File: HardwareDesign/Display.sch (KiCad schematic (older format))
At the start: 1 part, among them U601 Upduino_3.0

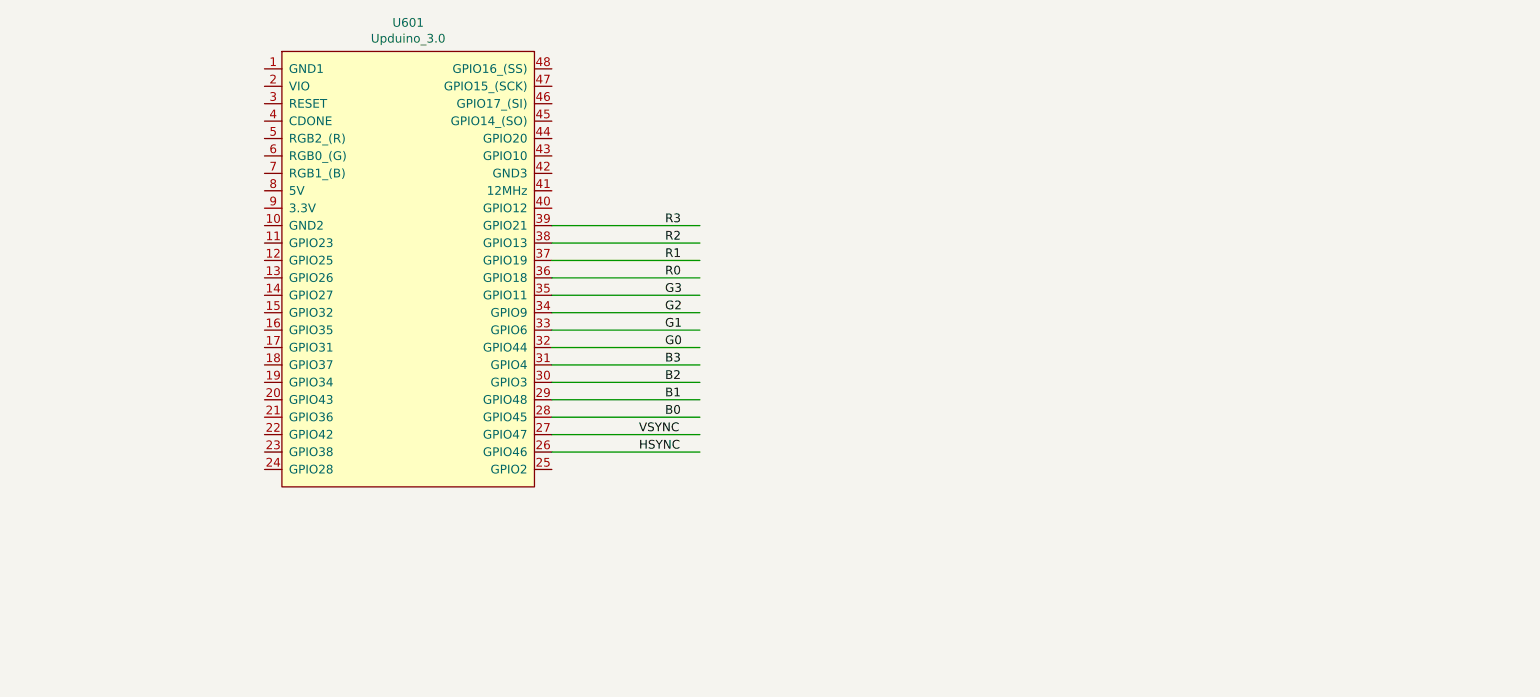
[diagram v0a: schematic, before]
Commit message: initial display circuit
The display isn't interfaced with the system yet.
Initial goal is to generate a valid 800x600 SVGA signal.

Added a footprint for the Upduino 3.0, which is DIP-48,
but 0.7" wide rather than the standard 0.6".
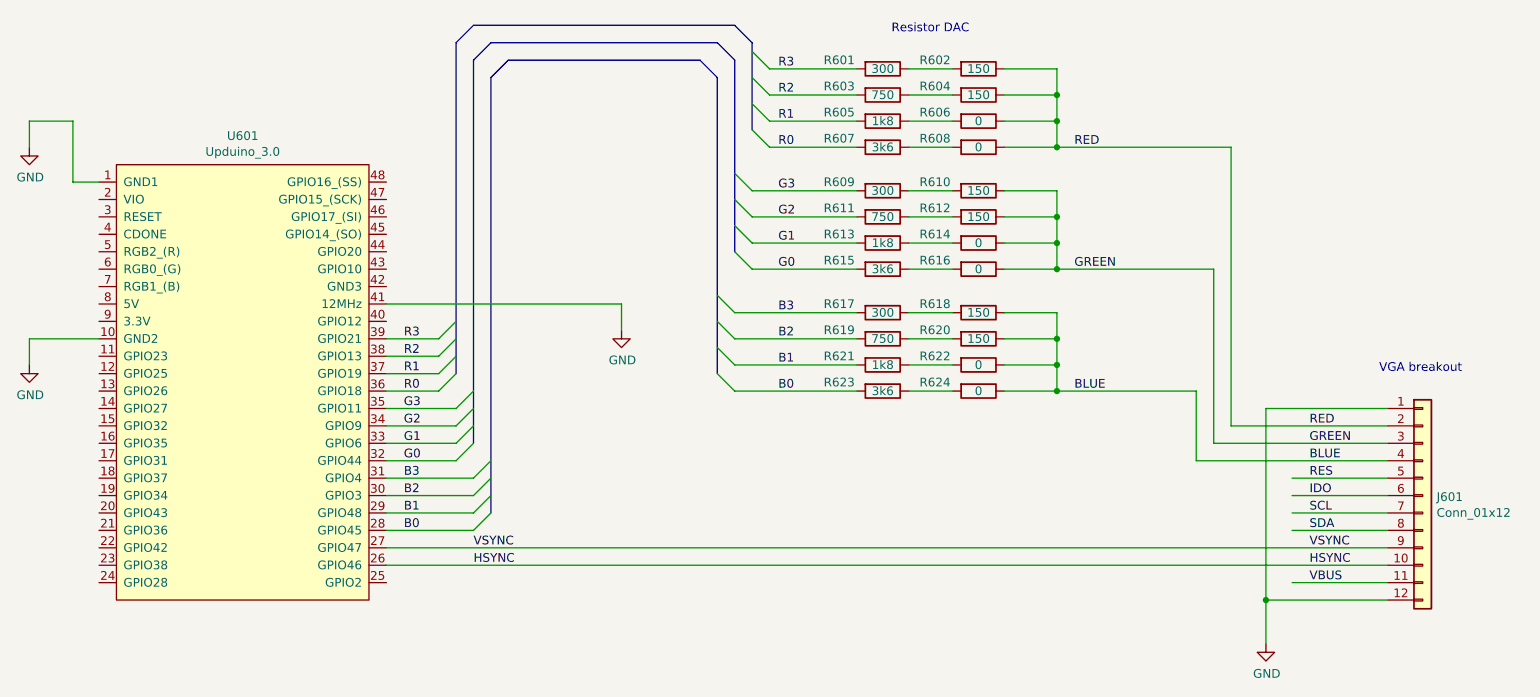
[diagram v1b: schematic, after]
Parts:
- added J601: Conn_01x12, symbol Connector_Generic:Conn_01x12
- added R601, R609, R617: 300, symbol device:R
- added R602, R604, R610, R612, R618, R620: 150, symbol device:R
- added R603, R611, R619: 750, symbol device:R
- added R605, R613, R621: 1k8, symbol device:R
- added R606, R608, R614, R616, R622, R624: 0, symbol device:R
- added R607, R615, R623: 3k6, symbol device:R
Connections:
- net labels added: BLUE, GND, GREEN, IDO, RED, RES, SCL, SDA, VBUS
- wire segments 14 -> 85
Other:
- note added: "Resistor DAC"
- note added: "VGA breakout"
- moved on the sheet: U601

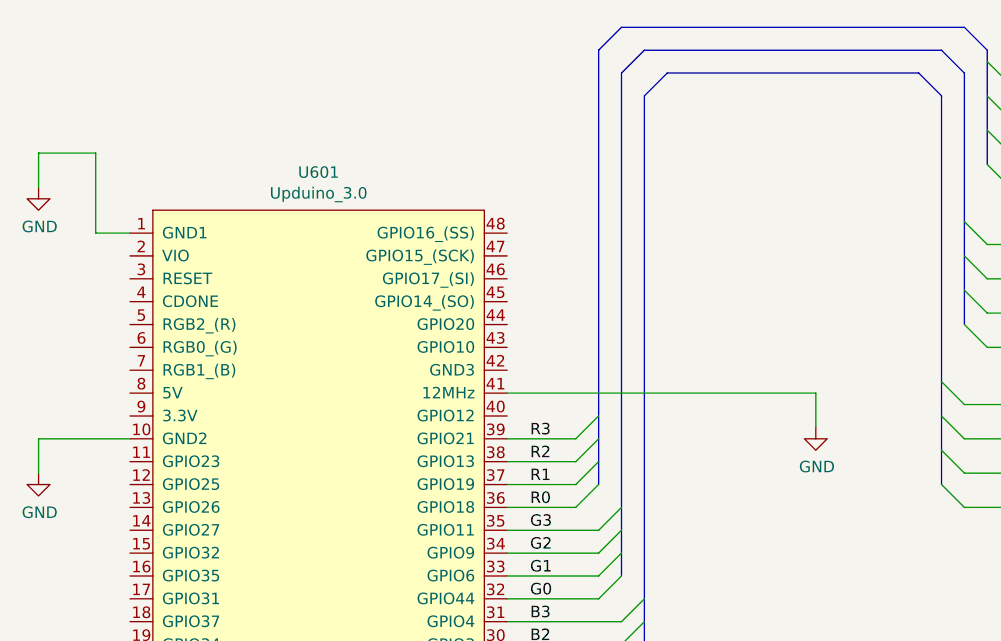
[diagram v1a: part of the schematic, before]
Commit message: corrected Upduino 3.0 pin assignments
The 12MHz and GND3 pins were accidentally reversed
on the silkscreen.
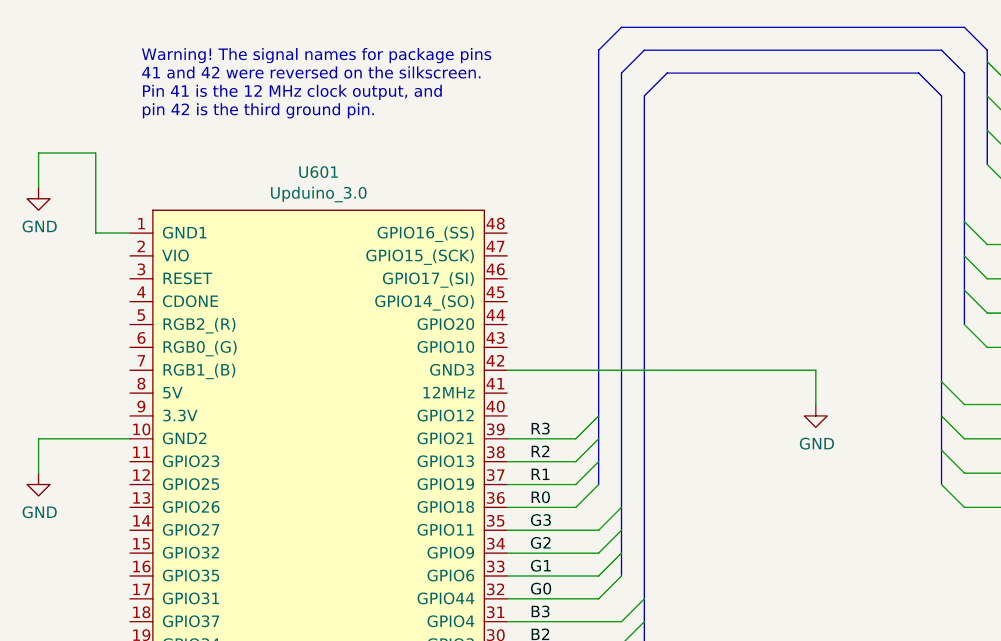
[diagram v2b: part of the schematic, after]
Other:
- note added: "Warning! The signal names for package pins\n41 and 42 were reversed on the silkscreen.\nPin 41 is the 12 MHz clock output, and\npin 42 is the third ground pin."
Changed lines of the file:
@@
 Comment4 ""
 $EndDescr
-$Comp
-L Upduino_3.0:Upduino_3.0 U601
-U 1 1 60B8636D
-P 2400 2400
-F 0 "U601" H 2375 2465 50  0000 C CNN
-F 1 "Upduino_3.0" H 2375 2374 50  0000 C CNN
-F 2 "" H 2400 2350 50  0001 C CNN
-F 3 "" H 2400 2350 50  0001 C CNN
-	1    2400 2400
-	1    0    0    -1
-$EndComp
 Text Label 3700 4700 0    50   ~ 0
 VSYNC
@@
 $EndComp
 Wire Wire Line
-	3200 3300 4550 3300
-Wire Wire Line
-	4550 3300 4550 3450
+	3200 3200 4550 3200
+Wire Wire Line
+	4550 3200 4550 3350
 $Comp
 L power:GND #PWR?
 U 1 1 60BF23D5
-P 4550 3450
-F 0 "#PWR?" H 4550 3200 50  0001 C CNN
-F 1 "GND" H 4555 3277 50  0000 C CNN
-F 2 "" H 4550 3450 50  0001 C CNN
-F 3 "" H 4550 3450 50  0001 C CNN
-	1    4550 3450
+P 4550 3350
+F 0 "#PWR?" H 4550 3100 50  0001 C CNN
+F 1 "GND" H 4555 3177 50  0000 C CNN
+F 2 "" H 4550 3350 50  0001 C CNN
+F 3 "" H 4550 3350 50  0001 C CNN
+	1    4550 3350
 	1    0    0    -1
 $EndComp
@@
 Entry Wire Line
 	5100 3700 5200 3800
+$Comp
+L Upduino_3.0:Upduino_3.0 U601
+U 1 1 60BB2F09
+P 2400 2400
+F 0 "U601" H 2375 2465 50  0000 C CNN
+F 1 "Upduino_3.0" H 2375 2374 50  0000 C CNN
+F 2 "" H 2400 2350 50  0001 C CNN
+F 3 "" H 2400 2350 50  0001 C CNN
+	1    2400 2400
+	1    0    0    -1
+$EndComp
 Wire Bus Line
 	5100 2000 5100 3700
@@
 Wire Bus Line
 	5300 1800 5300 2300
+Text Notes 1600 2100 0    50   ~ 0
+Warning! The signal names for package pins\n41 and 42 were reversed on the silkscreen.\nPin 41 is the 12 MHz clock output, and\npin 42 is the third ground pin.
 $EndSCHEMATC

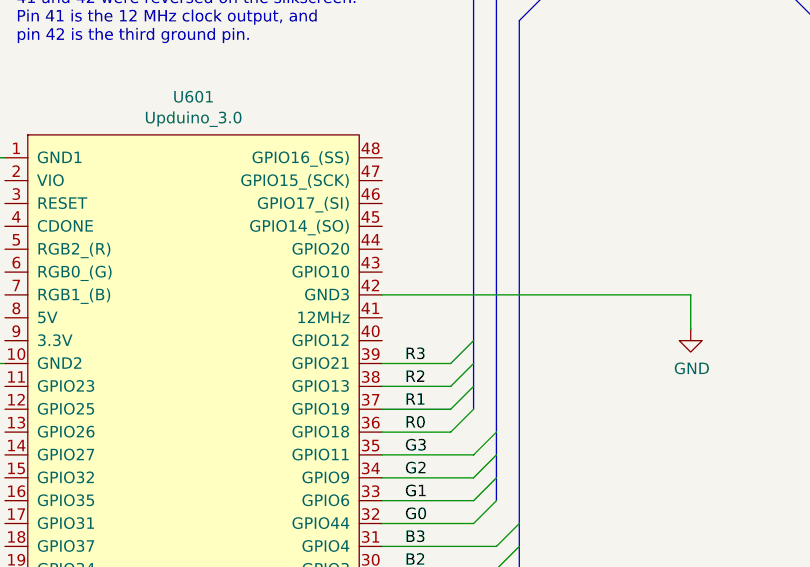
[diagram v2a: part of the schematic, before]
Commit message: connect 12 MHz clock to GPIO 20
The internal high-frequency oscillator is not very accurate,
and has significant jitter.
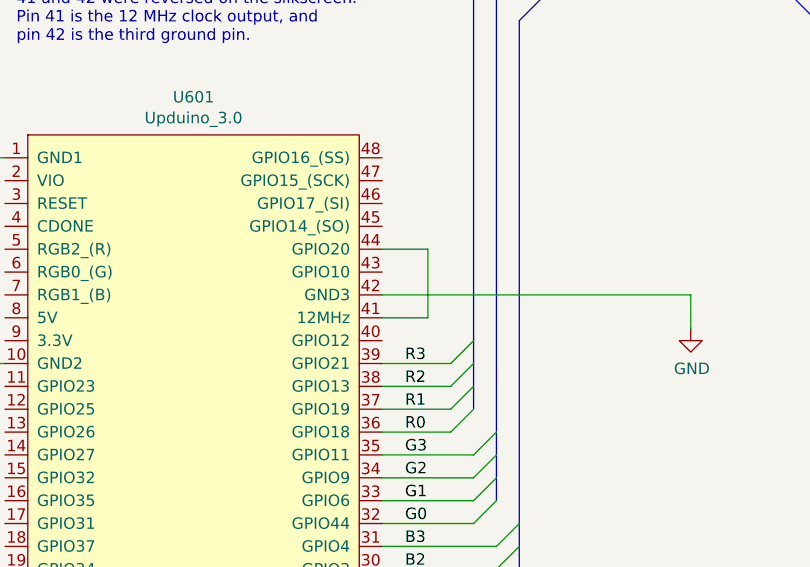
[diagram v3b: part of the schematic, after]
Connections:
- wire segments 85 -> 88
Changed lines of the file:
@@
 	1    0    0    -1
 $EndComp
+Text Notes 1600 2100 0    50   ~ 0
+Warning! The signal names for package pins\n41 and 42 were reversed on the silkscreen.\nPin 41 is the 12 MHz clock output, and\npin 42 is the third ground pin.
+Wire Wire Line
+	3200 3300 3400 3300
+Wire Wire Line
+	3400 3300 3400 3000
+Wire Wire Line
+	3400 3000 3200 3000
 Wire Bus Line
 	5100 2000 5100 3700
@@
 Wire Bus Line
 	5300 1800 5300 2300
-Text Notes 1600 2100 0    50   ~ 0
-Warning! The signal names for package pins\n41 and 42 were reversed on the silkscreen.\nPin 41 is the 12 MHz clock output, and\npin 42 is the third ground pin.
 $EndSCHEMATC

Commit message: associated more footprints
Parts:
- J601: footprint (none) -> Connector_PinHeader_2.54mm:PinHeader_1x12_P2.54mm_Vertical
- R601, R602, R603, R604, R605, R606, R607, R608, R609, R610, R611, R612, R613, R614, R615, R616, R617, R618, R619, R620, R621, R622, R623, R624: footprint (none) -> Resistor_THT:R_Axial_DIN0204_L3.6mm_D1.6mm_P7.62mm_Horizontal
- U601: footprint (none) -> HardwareDesign:DIP-48_W17.78mm
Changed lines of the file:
@@
 F 0 "R603" V 6000 1850 50  0000 C CNN
 F 1 "750" V 6050 2100 50  0000 C CNN
-F 2 "" V 5980 2100 50  0001 C CNN
+F 2 "Resistor_THT:R_Axial_DIN0204_L3.6mm_D1.6mm_P7.62mm_Horizontal" V 5980 2100 50  0001 C CNN
 F 3 "" H 6050 2100 50  0001 C CNN
 	1    6050 2100
@@
 F 0 "R601" V 6000 1700 50  0000 C CNN
 F 1 "300" V 6050 1950 50  0000 C CNN
-F 2 "" V 5980 1950 50  0001 C CNN
+F 2 "Resistor_THT:R_Axial_DIN0204_L3.6mm_D1.6mm_P7.62mm_Horizontal" V 5980 1950 50  0001 C CNN
 F 3 "" H 6050 1950 50  0001 C CNN
 	1    6050 1950
@@
 F 0 "R604" V 6550 1850 50  0000 C CNN
 F 1 "150" V 6600 2100 50  0000 C CNN
-F 2 "" V 6530 2100 50  0001 C CNN
+F 2 "Resistor_THT:R_Axial_DIN0204_L3.6mm_D1.6mm_P7.62mm_Horizontal" V 6530 2100 50  0001 C CNN
 F 3 "" H 6600 2100 50  0001 C CNN
 	1    6600 2100
@@
 F 0 "R602" V 6550 1700 50  0000 C CNN
 F 1 "150" V 6600 1950 50  0000 C CNN
-F 2 "" V 6530 1950 50  0001 C CNN
+F 2 "Resistor_THT:R_Axial_DIN0204_L3.6mm_D1.6mm_P7.62mm_Horizontal" V 6530 1950 50  0001 C CNN
 F 3 "" H 6600 1950 50  0001 C CNN
 	1    6600 1950
@@
 F 0 "R607" V 6000 2150 50  0000 C CNN
 F 1 "3k6" V 6050 2400 50  0000 C CNN
-F 2 "" V 5980 2400 50  0001 C CNN
+F 2 "Resistor_THT:R_Axial_DIN0204_L3.6mm_D1.6mm_P7.62mm_Horizontal" V 5980 2400 50  0001 C CNN
 F 3 "" H 6050 2400 50  0001 C CNN
 	1    6050 2400
@@
 F 0 "R605" V 6000 2000 50  0000 C CNN
 F 1 "1k8" V 6050 2250 50  0000 C CNN
-F 2 "" V 5980 2250 50  0001 C CNN
+F 2 "Resistor_THT:R_Axial_DIN0204_L3.6mm_D1.6mm_P7.62mm_Horizontal" V 5980 2250 50  0001 C CNN
 F 3 "" H 6050 2250 50  0001 C CNN
 	1    6050 2250
@@
 F 0 "R608" V 6550 2150 50  0000 C CNN
 F 1 "0" V 6600 2400 50  0000 C CNN
-F 2 "" V 6530 2400 50  0001 C CNN
+F 2 "Resistor_THT:R_Axial_DIN0204_L3.6mm_D1.6mm_P7.62mm_Horizontal" V 6530 2400 50  0001 C CNN
 F 3 "" H 6600 2400 50  0001 C CNN
 	1    6600 2400
@@
 F 0 "R606" V 6550 2000 50  0000 C CNN
 F 1 "0" V 6600 2250 50  0000 C CNN
-F 2 "" V 6530 2250 50  0001 C CNN
+F 2 "Resistor_THT:R_Axial_DIN0204_L3.6mm_D1.6mm_P7.62mm_Horizontal" V 6530 2250 50  0001 C CNN
 F 3 "" H 6600 2250 50  0001 C CNN
 	1    6600 2250
@@
 F 0 "R611" V 6000 2550 50  0000 C CNN
 F 1 "750" V 6050 2800 50  0000 C CNN
-F 2 "" V 5980 2800 50  0001 C CNN
+F 2 "Resistor_THT:R_Axial_DIN0204_L3.6mm_D1.6mm_P7.62mm_Horizontal" V 5980 2800 50  0001 C CNN
 F 3 "" H 6050 2800 50  0001 C CNN
 	1    6050 2800
@@
 F 0 "R609" V 6000 2400 50  0000 C CNN
 F 1 "300" V 6050 2650 50  0000 C CNN
-F 2 "" V 5980 2650 50  0001 C CNN
+F 2 "Resistor_THT:R_Axial_DIN0204_L3.6mm_D1.6mm_P7.62mm_Horizontal" V 5980 2650 50  0001 C CNN
 F 3 "" H 6050 2650 50  0001 C CNN
 	1    6050 2650
@@
 F 0 "R612" V 6550 2550 50  0000 C CNN
 F 1 "150" V 6600 2800 50  0000 C CNN
-F 2 "" V 6530 2800 50  0001 C CNN
+F 2 "Resistor_THT:R_Axial_DIN0204_L3.6mm_D1.6mm_P7.62mm_Horizontal" V 6530 2800 50  0001 C CNN
 F 3 "" H 6600 2800 50  0001 C CNN
 	1    6600 2800
@@
 F 0 "R610" V 6550 2400 50  0000 C CNN
 F 1 "150" V 6600 2650 50  0000 C CNN
-F 2 "" V 6530 2650 50  0001 C CNN
+F 2 "Resistor_THT:R_Axial_DIN0204_L3.6mm_D1.6mm_P7.62mm_Horizontal" V 6530 2650 50  0001 C CNN
 F 3 "" H 6600 2650 50  0001 C CNN
 	1    6600 2650
@@
 F 0 "R615" V 6000 2850 50  0000 C CNN
 F 1 "3k6" V 6050 3100 50  0000 C CNN
-F 2 "" V 5980 3100 50  0001 C CNN
+F 2 "Resistor_THT:R_Axial_DIN0204_L3.6mm_D1.6mm_P7.62mm_Horizontal" V 5980 3100 50  0001 C CNN
 F 3 "" H 6050 3100 50  0001 C CNN
 	1    6050 3100
@@
 F 0 "R613" V 6000 2700 50  0000 C CNN
 F 1 "1k8" V 6050 2950 50  0000 C CNN
-F 2 "" V 5980 2950 50  0001 C CNN
+F 2 "Resistor_THT:R_Axial_DIN0204_L3.6mm_D1.6mm_P7.62mm_Horizontal" V 5980 2950 50  0001 C CNN
 F 3 "" H 6050 2950 50  0001 C CNN
 	1    6050 2950
@@
 F 0 "R616" V 6550 2850 50  0000 C CNN
 F 1 "0" V 6600 3100 50  0000 C CNN
-F 2 "" V 6530 3100 50  0001 C CNN
+F 2 "Resistor_THT:R_Axial_DIN0204_L3.6mm_D1.6mm_P7.62mm_Horizontal" V 6530 3100 50  0001 C CNN
 F 3 "" H 6600 3100 50  0001 C CNN
 	1    6600 3100
@@
 F 0 "R614" V 6550 2700 50  0000 C CNN
 F 1 "0" V 6600 2950 50  0000 C CNN
-F 2 "" V 6530 2950 50  0001 C CNN
+F 2 "Resistor_THT:R_Axial_DIN0204_L3.6mm_D1.6mm_P7.62mm_Horizontal" V 6530 2950 50  0001 C CNN
 F 3 "" H 6600 2950 50  0001 C CNN
 	1    6600 2950
@@
 F 0 "R619" V 6000 3250 50  0000 C CNN
 F 1 "750" V 6050 3500 50  0000 C CNN
-F 2 "" V 5980 3500 50  0001 C CNN
+F 2 "Resistor_THT:R_Axial_DIN0204_L3.6mm_D1.6mm_P7.62mm_Horizontal" V 5980 3500 50  0001 C CNN
 F 3 "" H 6050 3500 50  0001 C CNN
 	1    6050 3500
@@
 F 0 "R617" V 6000 3100 50  0000 C CNN
 F 1 "300" V 6050 3350 50  0000 C CNN
-F 2 "" V 5980 3350 50  0001 C CNN
+F 2 "Resistor_THT:R_Axial_DIN0204_L3.6mm_D1.6mm_P7.62mm_Horizontal" V 5980 3350 50  0001 C CNN
 F 3 "" H 6050 3350 50  0001 C CNN
 	1    6050 3350
@@
 F 0 "R620" V 6550 3250 50  0000 C CNN
 F 1 "150" V 6600 3500 50  0000 C CNN
-F 2 "" V 6530 3500 50  0001 C CNN
+F 2 "Resistor_THT:R_Axial_DIN0204_L3.6mm_D1.6mm_P7.62mm_Horizontal" V 6530 3500 50  0001 C CNN
 F 3 "" H 6600 3500 50  0001 C CNN
 	1    6600 3500
@@
 F 0 "R618" V 6550 3100 50  0000 C CNN
 F 1 "150" V 6600 3350 50  0000 C CNN
-F 2 "" V 6530 3350 50  0001 C CNN
+F 2 "Resistor_THT:R_Axial_DIN0204_L3.6mm_D1.6mm_P7.62mm_Horizontal" V 6530 3350 50  0001 C CNN
 F 3 "" H 6600 3350 50  0001 C CNN
 	1    6600 3350
@@
 F 0 "R623" V 6000 3550 50  0000 C CNN
 F 1 "3k6" V 6050 3800 50  0000 C CNN
-F 2 "" V 5980 3800 50  0001 C CNN
+F 2 "Resistor_THT:R_Axial_DIN0204_L3.6mm_D1.6mm_P7.62mm_Horizontal" V 5980 3800 50  0001 C CNN
 F 3 "" H 6050 3800 50  0001 C CNN
 	1    6050 3800
@@
 F 0 "R621" V 6000 3400 50  0000 C CNN
 F 1 "1k8" V 6050 3650 50  0000 C CNN
-F 2 "" V 5980 3650 50  0001 C CNN
+F 2 "Resistor_THT:R_Axial_DIN0204_L3.6mm_D1.6mm_P7.62mm_Horizontal" V 5980 3650 50  0001 C CNN
 F 3 "" H 6050 3650 50  0001 C CNN
 	1    6050 3650
@@
 F 0 "R624" V 6550 3550 50  0000 C CNN
 F 1 "0" V 6600 3800 50  0000 C CNN
-F 2 "" V 6530 3800 50  0001 C CNN
+F 2 "Resistor_THT:R_Axial_DIN0204_L3.6mm_D1.6mm_P7.62mm_Horizontal" V 6530 3800 50  0001 C CNN
 F 3 "" H 6600 3800 50  0001 C CNN
 	1    6600 3800
@@
 F 0 "R622" V 6550 3400 50  0000 C CNN
 F 1 "0" V 6600 3650 50  0000 C CNN
-F 2 "" V 6530 3650 50  0001 C CNN
+F 2 "Resistor_THT:R_Axial_DIN0204_L3.6mm_D1.6mm_P7.62mm_Horizontal" V 6530 3650 50  0001 C CNN
 F 3 "" H 6600 3650 50  0001 C CNN
 	1    6600 3650
@@
 F 0 "J601" H 9230 4392 50  0000 L CNN
 F 1 "Conn_01x12" H 9230 4301 50  0000 L CNN
-F 2 "" H 9150 4400 50  0001 C CNN
+F 2 "Connector_PinHeader_2.54mm:PinHeader_1x12_P2.54mm_Vertical" H 9150 4400 50  0001 C CNN
 F 3 "~" H 9150 4400 50  0001 C CNN
 	1    9150 4400
@@
 	8250 5000 8250 5250
 $Comp
-L power:GND #PWR?
+L power:GND #PWR0137
 U 1 1 60BE62A3
 P 8250 5250
-F 0 "#PWR?" H 8250 5000 50  0001 C CNN
+F 0 "#PWR0137" H 8250 5000 50  0001 C CNN
 F 1 "GND" H 8255 5077 50  0000 C CNN
 F 2 "" H 8250 5250 50  0001 C CNN
@@
 	1150 2250 1150 2400
 $Comp
-L power:GND #PWR?
+L power:GND #PWR0191
 U 1 1 60BED77C
 P 1150 2400
-F 0 "#PWR?" H 1150 2150 50  0001 C CNN
+F 0 "#PWR0191" H 1150 2150 50  0001 C CNN
 F 1 "GND" H 1155 2227 50  0000 C CNN
 F 2 "" H 1150 2400 50  0001 C CNN
@@
 	4550 3200 4550 3350
 $Comp
-L power:GND #PWR?
+L power:GND #PWR0192
 U 1 1 60BF23D5
 P 4550 3350
-F 0 "#PWR?" H 4550 3100 50  0001 C CNN
+F 0 "#PWR0192" H 4550 3100 50  0001 C CNN
 F 1 "GND" H 4555 3177 50  0000 C CNN
 F 2 "" H 4550 3350 50  0001 C CNN
@@
 	1150 3500 1150 3650
 $Comp
-L power:GND #PWR?
+L power:GND #PWR0193
 U 1 1 60BF690E
 P 1150 3650
-F 0 "#PWR?" H 1150 3400 50  0001 C CNN
+F 0 "#PWR0193" H 1150 3400 50  0001 C CNN
 F 1 "GND" H 1155 3477 50  0000 C CNN
 F 2 "" H 1150 3650 50  0001 C CNN
@@
 F 0 "U601" H 2375 2465 50  0000 C CNN
 F 1 "Upduino_3.0" H 2375 2374 50  0000 C CNN
-F 2 "" H 2400 2350 50  0001 C CNN
+F 2 "HardwareDesign:DIP-48_W17.78mm" H 2400 2350 50  0001 C CNN
 F 3 "" H 2400 2350 50  0001 C CNN
 	1    2400 2400
